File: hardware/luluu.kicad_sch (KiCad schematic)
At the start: 47 parts, among them CN1 DISP_LCD_ST7789, J1 USB_C_Receptacle_USB2.0, J2 STEMMA_{QT} I_{2}C (JST SH), J3 Micro_SD_Card, J4 BATT_CON, J5 SWD_PI_3WIRE, J6 UART_PI_3WIRE, Q1 DMG3415UFY4Q-7, Q2 BSS138, SW1 SW_USBBOOT, SW2 SW_RESET, U1 RP2040, U2 MCP73831-2-OT, U3 RT9080-33GJ5, U4 APX803, U6 W25Q64JVSS, Y1 TX322512M4LBCE2T

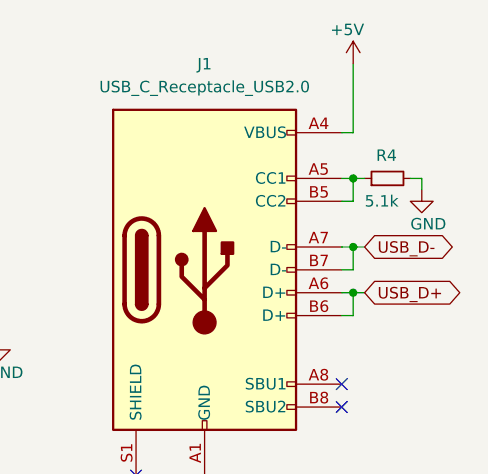
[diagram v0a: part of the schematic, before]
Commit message: fix usb cc resistor
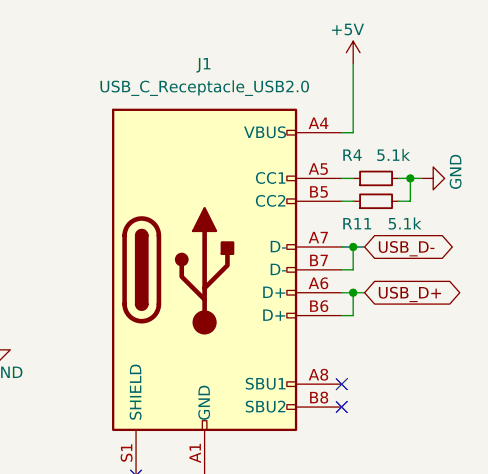
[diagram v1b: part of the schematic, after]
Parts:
- added R11: 5.1k, symbol Device:R_Small
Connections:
- net GND: now also R11.2
- net at J1.A5 (CC1), R4.1: no longer J1.B5 (CC2)
- new net: J1.B5 (CC2), R11.1
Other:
- moved on the sheet: R4
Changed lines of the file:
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@@
   (junction (at 170.18 91.44) (diameter 0) (color 0 0 0 0)
   )
+  (junction (at 274.32 33.02) (diameter 0) (color 0 0 0 0)
+  )
   (junction (at 254 133.35) (diameter 0) (color 0 0 0 0)
   )
@@
   (junction (at 106.68 68.58) (diameter 0) (color 0 0 0 0)
   )
-  (junction (at 267.97 33.02) (diameter 0) (color 0 0 0 0)
-  )
   (junction (at 110.49 68.58) (diameter 0) (color 0 0 0 0)
   )
@@
     (stroke (width 0) (type default))
   )
-  (wire (pts (xy 267.97 35.56) (xy 267.97 33.02))
-    (stroke (width 0) (type default))
-  )
   (wire (pts (xy 180.34 91.44) (xy 180.34 93.98))
     (stroke (width 0) (type default))
@@
     (stroke (width 0) (type default))
   )
-  (wire (pts (xy 274.32 33.02) (xy 275.59 33.02))
+  (wire (pts (xy 273.05 33.02) (xy 274.32 33.02))
     (stroke (width 0) (type default))
   )
@@
     (stroke (width 0) (type default))
   )
+  (wire (pts (xy 274.32 33.02) (xy 274.32 35.56))
+    (stroke (width 0) (type default))
+  )
   (wire (pts (xy 40.64 153.67) (xy 49.53 153.67))
     (stroke (width 0) (type default))
@@
     (stroke (width 0) (type default))
   )
+  (wire (pts (xy 274.32 33.02) (xy 275.59 33.02))
+    (stroke (width 0) (type default))
+  )
   (wire (pts (xy 19.05 121.92) (xy 20.32 121.92))
     (stroke (width 0) (type default))
@@
     (stroke (width 0) (type default))
   )
+  (wire (pts (xy 273.05 35.56) (xy 274.32 35.56))
+    (stroke (width 0) (type default))
+  )
   (wire (pts (xy 34.29 35.56) (xy 34.29 44.45))
     (stroke (width 0) (type default))
@@
     (stroke (width 0) (type default))
   )
-  (wire (pts (xy 275.59 33.02) (xy 275.59 34.29))
-    (stroke (width 0) (type default))
-  )
   (wire (pts (xy 110.49 74.93) (xy 110.49 76.2))
     (stroke (width 0) (type default))
@@
     (stroke (width 0) (type default))
   )
-  (wire (pts (xy 269.24 33.02) (xy 267.97 33.02))
-    (stroke (width 0) (type default))
-  )
   (wire (pts (xy 41.91 102.87) (xy 41.91 114.3))
     (stroke (width 0) (type default))
@@
     )
   )
+  (symbol (lib_id "Device:R_Small") (at 270.51 35.56 90) (unit 1)
+    (in_bom yes) (on_board yes) (dnp no)
+    (property "Reference" "R11" (at 266.7 38.1 90)
+      (effects (font (size 1.27 1.27)) (justify right))
+    )
+    (property "Value" "5.1k" (at 271.78 38.1 90)
+      (effects (font (size 1.27 1.27)) (justify right))
+    )
+    (property "Footprint" "" (at 270.51 35.56 0)
+      (effects (font (size 1.27 1.27)) hide)
+    )
+    (property "Datasheet" "~" (at 270.51 35.56 0)
+      (effects (font (size 1.27 1.27)) hide)
+    )
+    (pin "1")
+    (pin "2")
+    (instances
+      (project "luluu"
+        (path "/74934858-45e0-400e-9259-85b77d199d77"
+          (reference "R11") (unit 1)
+        )
+      )
+    )
+  )
   (symbol (lib_id "Device:C_Small") (at 119.38 87.63 0) (unit 1)
     (in_bom yes) (on_board yes) (dnp no) (fields_autoplaced)
@@
     )
   )
-  (symbol (lib_id "Device:R_Small") (at 271.78 33.02 90) (unit 1)
+  (symbol (lib_id "Device:R_Small") (at 270.51 33.02 90) (unit 1)
     (in_bom yes) (on_board yes) (dnp no)
-    (property "Reference" "R4" (at 270.51 30.48 90)
+    (property "Reference" "R4" (at 266.7 30.48 90)
       (effects (font (size 1.27 1.27)) (justify right))
     )
-    (property "Value" "5.1k" (at 269.24 35.56 90)
+    (property "Value" "5.1k" (at 270.51 30.48 90)
       (effects (font (size 1.27 1.27)) (justify right))
     )
-    (property "Footprint" "" (at 271.78 33.02 0)
+    (property "Footprint" "" (at 270.51 33.02 0)
       (effects (font (size 1.27 1.27)) hide)
     )
-    (property "Datasheet" "~" (at 271.78 33.02 0)
+    (property "Datasheet" "~" (at 270.51 33.02 0)
       (effects (font (size 1.27 1.27)) hide)
     )
@@
     )
   )
-  (symbol (lib_id "power:GND") (at 275.59 34.29 0) (unit 1)
+  (symbol (lib_id "power:GND") (at 275.59 33.02 90) (unit 1)
     (in_bom yes) (on_board yes) (dnp no)
-    (property "Reference" "#PWR017" (at 275.59 40.64 0)
+    (property "Reference" "#PWR017" (at 281.94 33.02 0)
       (effects (font (size 1.27 1.27)) hide)
     )
-    (property "Value" "GND" (at 274.32 38.1 0)
+    (property "Value" "GND" (at 279.4 34.29 0)
       (effects (font (size 1.27 1.27)) (justify left))
     )
-    (property "Footprint" "" (at 275.59 34.29 0)
+    (property "Footprint" "" (at 275.59 33.02 0)
       (effects (font (size 1.27 1.27)) hide)
     )
-    (property "Datasheet" "" (at 275.59 34.29 0)
+    (property "Datasheet" "" (at 275.59 33.02 0)
       (effects (font (size 1.27 1.27)) hide)
     )

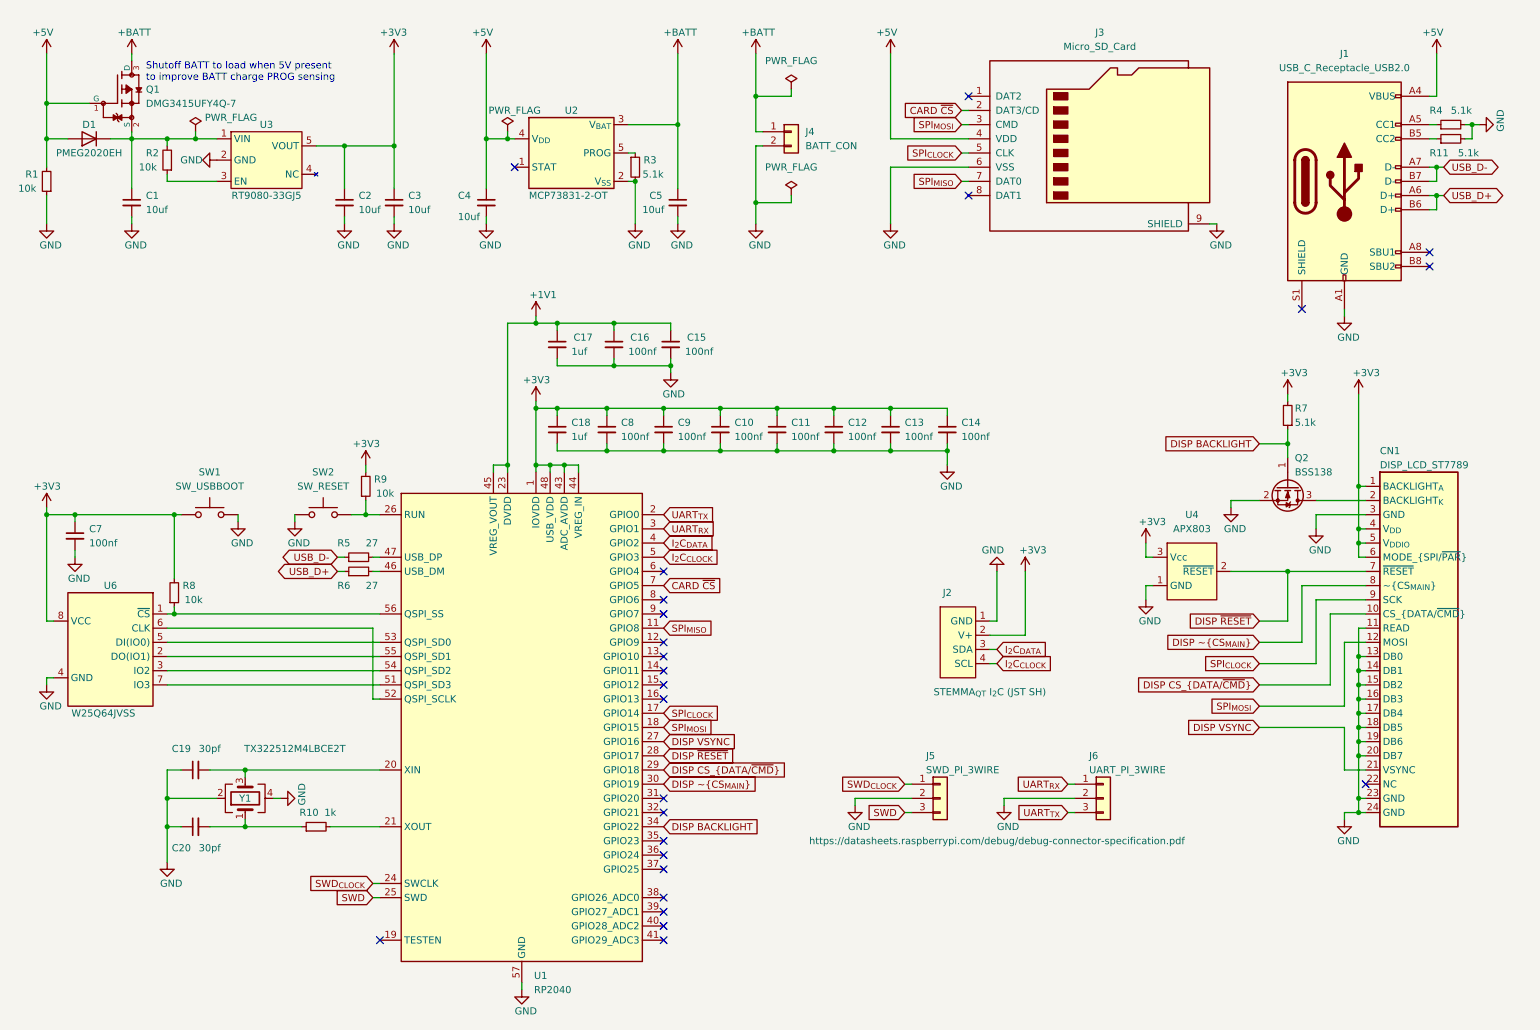
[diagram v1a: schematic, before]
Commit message: re-annotate, add display decoupling caps
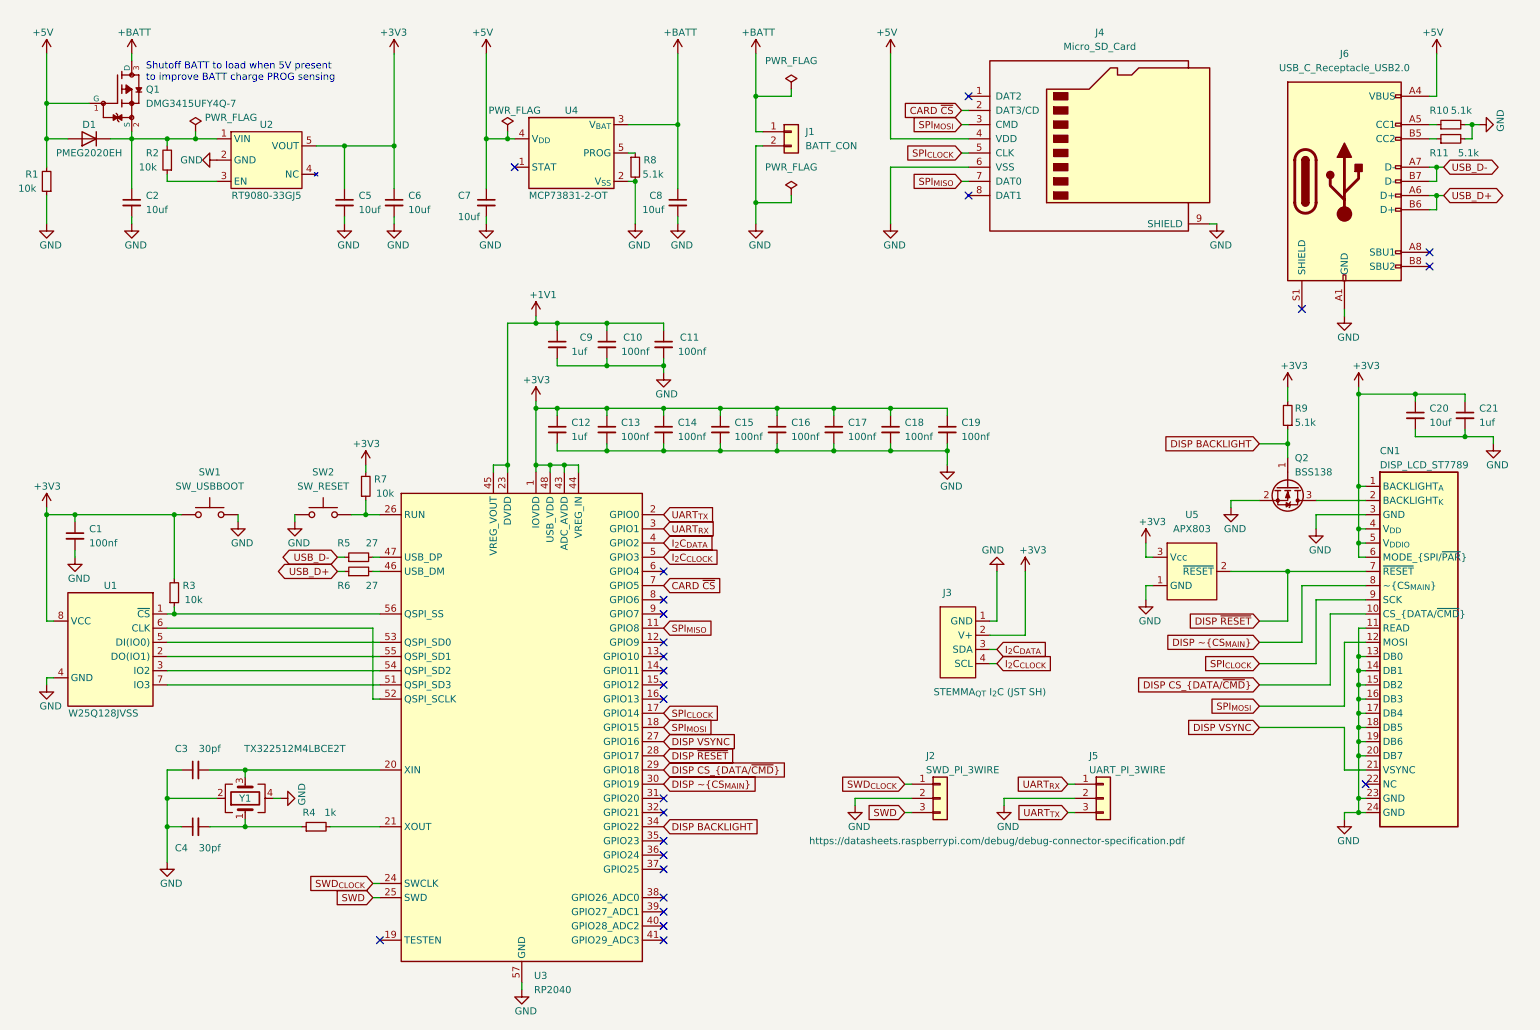
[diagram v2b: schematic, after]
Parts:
- added C20: 10uf, Capacitor_SMD:C_0603_1608Metric_Pad1.08x0.95mm_HandSolder, symbol Device:C_Small
- added C21: 1uf, Capacitor_SMD:C_0603_1608Metric_Pad1.08x0.95mm_HandSolder, symbol Device:C_Small
- U1: renamed from U6; value W25Q64JVSS -> W25Q128JVSS; symbol luluu:W25Q64JVSS -> luluu:W25QXXJVSS
- renumbered C7 to C1, C16 to C10, C15 to C11, C18 to C12, C8 to C13, C9 to C14, C10 to C15, C11 to C16, C12 to C17, C13 to C18, C14 to C19, C1 to C2, C19 to C3, C20 to C4, C2 to C5, C3 to C6, C4 to C7, C5 to C8, C17 to C9, J4 to J1, J5 to J2, J2 to J3, J3 to J4, J6 to J5, J1 to J6, R4 to R10, R8 to R3, R10 to R4, R9 to R7, R3 to R8, R7 to R9, U3 to U2, U1 to U3, U2 to U4, U4 to U5
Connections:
- net +3V3: now also C20.1, C21.1
- net GND: now also C20.2, C21.2
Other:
- moved on the sheet: C10, C11

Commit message: lots of updates
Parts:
- added C22: 10uf, Capacitor_SMD:C_0603_1608Metric_Pad1.08x0.95mm_HandSolder, symbol Device:C_Small
- added R12: 10, Resistor_SMD:R_0603_1608Metric_Pad0.98x0.95mm_HandSolder, symbol Device:R_Small
- added SW3: SW_POWER, Button_Switch_SMD:SW_SPDT_PCM12, symbol Switch:SW_SPST
- C1, C10, C11, C13, C14, C15, C16, C17, C18, C19: LCSC (none) -> C1525
- C12, C9: LCSC (none) -> C15849
- C2, C20, C5, C6, C7, C8: LCSC (none) -> C96446
- C21: value 1uf -> 100nf; footprint Capacitor_SMD:C_0603_1608Metric_Pad1.08x0.95mm_HandSolder -> Capacitor_SMD:C_0402_1005Metric_Pad0.74x0.62mm_HandSolder; LCSC (none) -> C1525
- C3, C4: LCSC (none) -> C1570
- D1: value PMEG2020EH -> SS34; footprint (none) -> Diode_SMD:D_SMA_Handsoldering; LCSC (none) -> C8678
- J4: LCSC (none) -> C585350
- J6: LCSC (none) -> C2988369
- J7: renamed from CN1; footprint (none) -> luluu:FPC_24_JUSHUO_AFC04-S24XCA-00; Connector Datasheet (none) -> https://datasheet.lcsc.com/lcsc/2010201934_JUSHUO-AFC04-S24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; LCSC (none) -> C883644
- Q1: value DMG3415UFY4Q-7 -> AO3401A; footprint luluu:TRANS_DMG3415UFY4Q-7 -> Package_TO_SOT_SMD:SOT-23; symbol luluu:DMG3415UFY4Q-7 -> Transistor_FET:AO3401A; LCSC (none) -> C15127
- Q2: LCSC (none) -> C7420339
- R1, R2, R3, R7: footprint (none) -> Resistor_SMD:R_0603_1608Metric_Pad0.98x0.95mm_HandSolder; LCSC (none) -> C25804
- R10, R11, R8, R9: footprint (none) -> Resistor_SMD:R_0603_1608Metric_Pad0.98x0.95mm_HandSolder; LCSC (none) -> C23186
- R4: footprint (none) -> Resistor_SMD:R_0603_1608Metric_Pad0.98x0.95mm_HandSolder; LCSC (none) -> C21190
- R5, R6: footprint (none) -> Resistor_SMD:R_0603_1608Metric_Pad0.98x0.95mm_HandSolder; LCSC (none) -> C25190
- SW1, SW2: footprint luluu:TS-1187A-B-A-B -> Button_Switch_SMD:SW_Push_1P1T_XKB_TS-1187A; LCSC (none) -> C318884
- U1: LCSC (none) -> C97521
- U2: LCSC (none) -> C841192
- U3: LCSC (none) -> C2040
- U4: value MCP73831-2-OT -> TP4054-42; symbol luluu:MCP73831-2-OT -> luluu:TP4054-42; LCSC (none) -> C32574
- U5: LCSC (none) -> C526393
- Y1: value TX322512M4LBCE2T -> X322512MSB4SI; LCSC (none) -> C9002
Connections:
- net +3V3: now also J4.4 (VDD), C22.1
- net +5V: no longer J4.4 (VDD)
- net GND: now also C22.2, SW3.2 (B); no longer J1.2 (Pin_2)
- net at Q2.3 (D): now also R12.1; no longer J7.2 (BACKLIGHT_{K})
- new net: J1.2 (Pin_2), SW3.1 (A)
- new net: J7.2 (BACKLIGHT_{K}), R12.2
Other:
- note added: "3V3 Power Reg"
- note added: "Battery Management"
- note added: "Connector specified by Adafruit STEMMA_{QT}"
- note added: "Connectors specified by RPi Debug Connector Specification"
- note added: "Crystal"
- note added: "Debug"
- note added: "Designed for 20pf spec'd load capacitance xtal"
- note added: "Display"
- note added: "Main RP2040"
- note added: "Must be Winbond W25QXXX Series"
- note added: "QSPI Flash"
- note added: "RP2040 I/O Pins"
- note added: "RP2040 Specified Bypass Caps"
- note added: "Reset Switches"
- note added: "STEMMA_{QT}"
- note added: "Shutoff BATT to load when 5V present to improve BATT charge sensing"
- note added: "USB Plug"
- note added: "microSD Card"
- note removed: "Shutoff BATT to load when 5V present to improve BATT charge PROG sensing"
- moved on the sheet: C2, C5, C6, C7, C8, D1, J1, J2, J3, J4, J5, Q2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

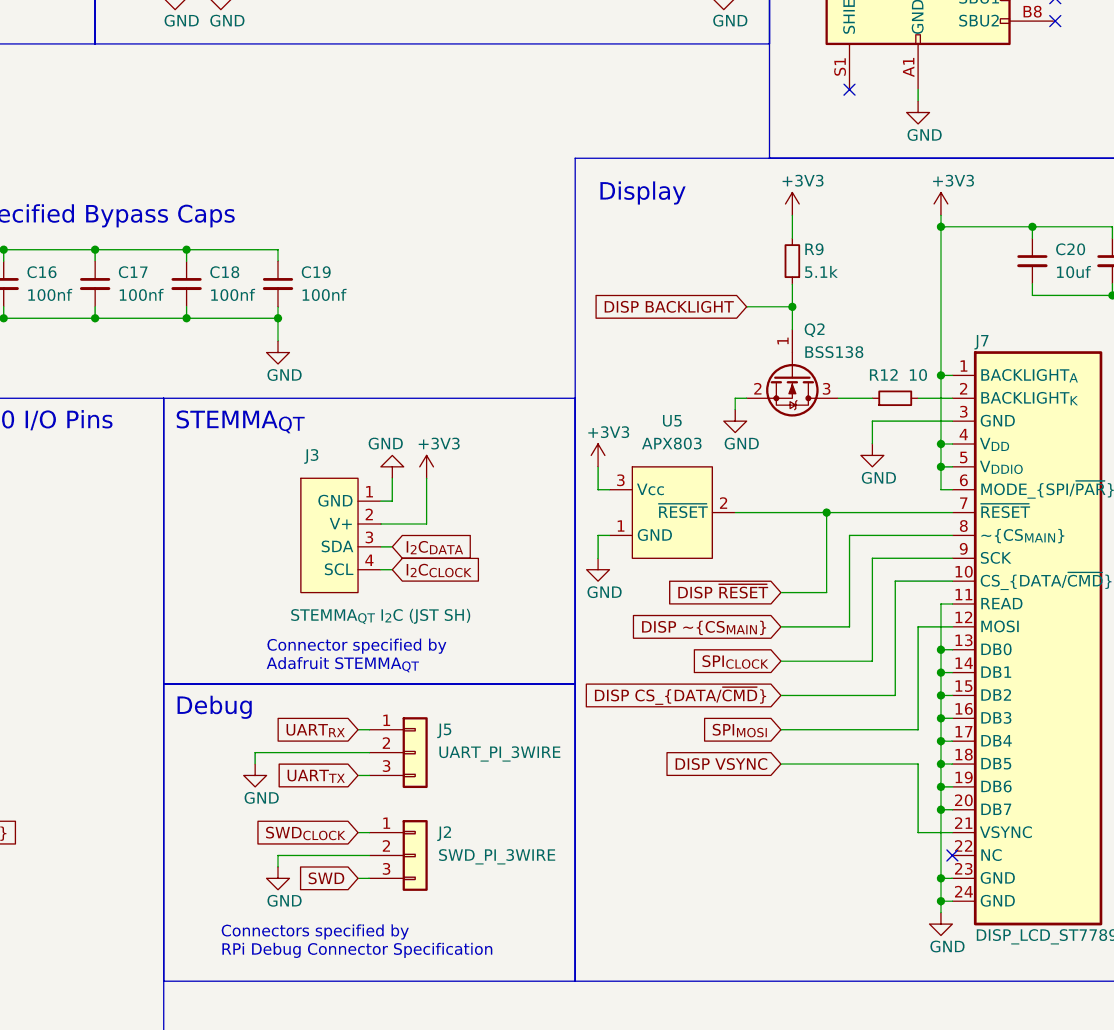
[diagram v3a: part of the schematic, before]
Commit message: update footprints and sourcing
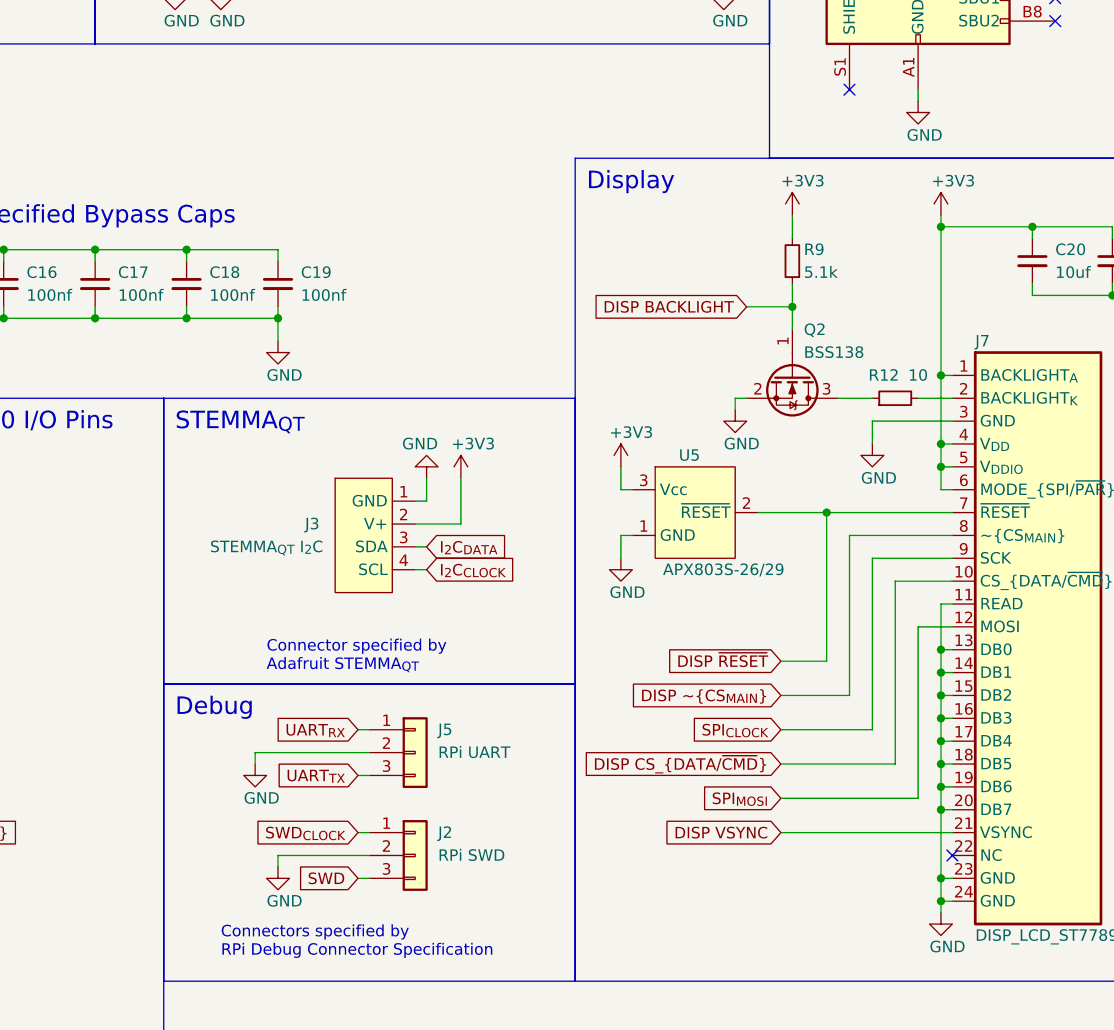
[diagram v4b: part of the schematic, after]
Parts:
- J1: footprint Connector_JST:JST_PH_S2B-PH-K_1x02_P2.00mm_Horizontal -> Connector_JST:JST_PH_S2B-PH-SM4-TB_1x02-1MP_P2.00mm_Horizontal; Farnell OC (none) -> 9492615
- J2: value SWD_PI_3WIRE -> RPi SWD; Farnell OC (none) -> 1679128
- J3: value STEMMA_{QT} I_{2}C (JST SH) -> STEMMA_{QT} I_{2}C; Farnell OC (none) -> 1830839
- J5: value UART_PI_3WIRE -> RPi UART; Farnell OC (none) -> 1679128
- J7: footprint luluu:FPC_24_JUSHUO_AFC04-S24XCA-00 -> luluu:FPC_24_SOLDER; Connector Datasheet https://datasheet.lcsc.com/lcsc/2010201934_JUSHUO-AFC04-S24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 -> (none); Farnell OC (none) -> 3385226; LCSC C883644 -> (none)
- SW3: Farnell OC (none) -> 9575146; LCSC C2911519 -> (none)
- U5: value APX803 -> APX803S-26/29
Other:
- moved on the sheet: J3, U5
